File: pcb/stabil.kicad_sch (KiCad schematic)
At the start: 42 parts, among them Q10 IRFR5305, U11 TPS5430DDA, U12 LM75B, U13 INA219AxD, U14 LM78M05_TO252, U16 TSV911IDT, U17 PC817, U18 LM75B

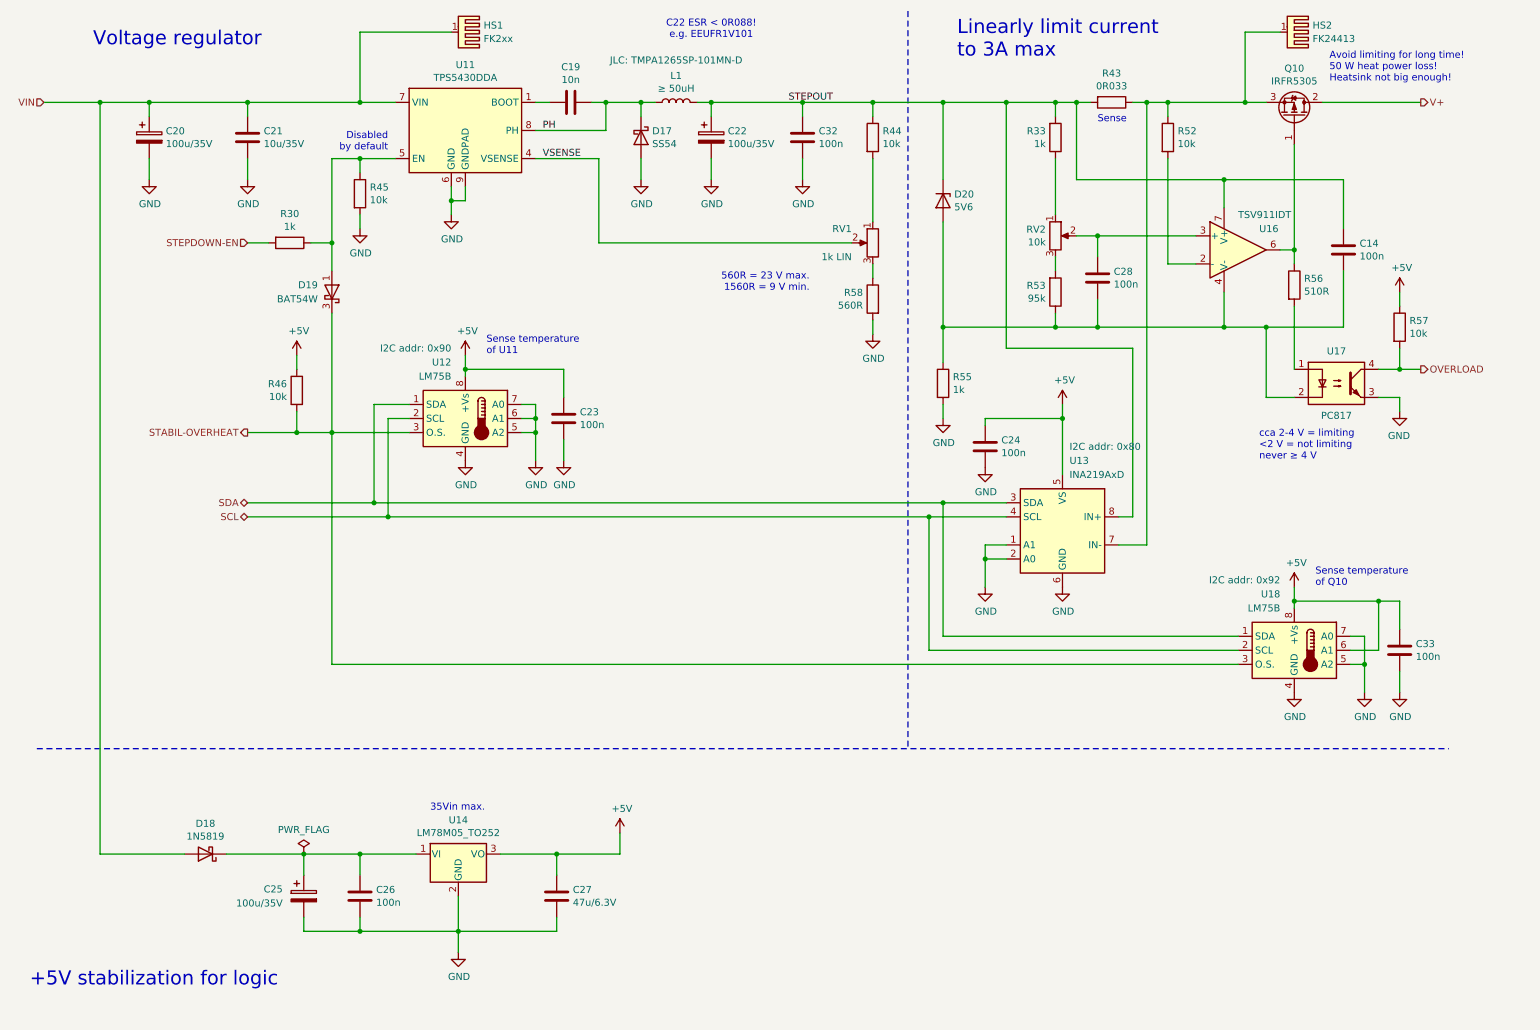
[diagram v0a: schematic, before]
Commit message: Use switched power supply for 5V internal.
78M05 would have 2.5 W of heat loss on it @ 30V input.
Other minor improvements.
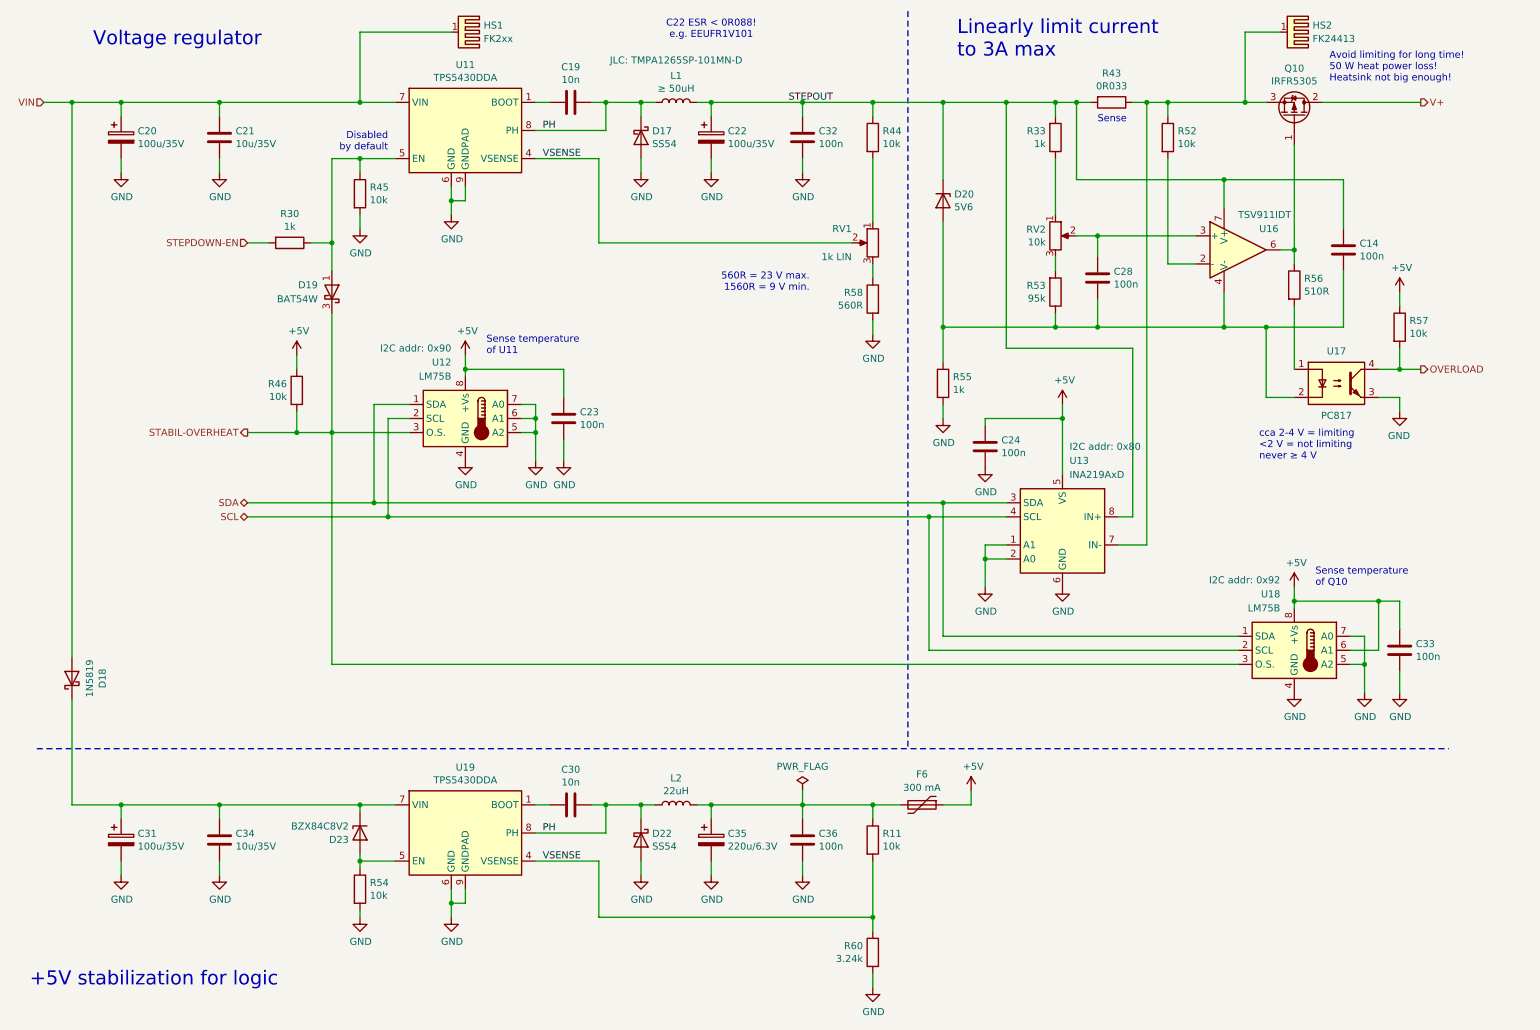
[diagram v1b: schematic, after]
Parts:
- removed C25: 100u/35V, Capacitor_THT:CP_Radial_D6.3mm_P2.50mm, symbol Device:C_Polarized
- removed C26: 100n, Capacitor_SMD:C_0805_2012Metric, symbol Device:C
- removed C27: 47u/6.3V, Capacitor_SMD:C_0805_2012Metric, symbol Device:C
- removed U14: LM78M05_TO252, Package_TO_SOT_SMD:TO-252-2, symbol Regulator_Linear:LM78M05_TO252
- added C30: 10n, Capacitor_SMD:C_0805_2012Metric, symbol Device:C
- added C31: 100u/35V, Capacitor_THT:CP_Radial_D6.3mm_P2.50mm, symbol Device:C_Polarized
- added C34: 10u/35V, Capacitor_SMD:C_0805_2012Metric, symbol Device:C
- added C35: 220u/6.3V, Capacitor_THT:CP_Radial_D8.0mm_P3.50mm, symbol Device:C_Polarized
- added C36: 100n, Capacitor_SMD:C_0805_2012Metric, symbol Device:C
- added D22: SS54, Diode_SMD:D_SMA, symbol Device:D_Schottky
- added D23: BZX84C8V2, Package_TO_SOT_SMD:SOT-23, symbol Diode:BZX84Cxx
- added F6: 300 mA, Fuse:Fuse_2920_7451Metric, symbol Device:Polyfuse
- added L2: 22uH, Inductor_SMD:L_Changjiang_FNR4020S, symbol Device:L
- added R11, R54: 10k, Resistor_SMD:R_0805_2012Metric, symbol Device:R
- added R60: 3.24k, Resistor_SMD:R_0805_2012Metric, symbol Device:R
- added U19: TPS5430DDA, Package_SO:TI_SO-PowerPAD-8_ThermalVias, symbol Regulator_Switching:TPS5430DDA
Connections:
- net +5V: now also F6.1
- net GND: now also C31.2, C34.2, C35.2, C36.2, D22.2 (A), R54.2, R60.2, U19.6 (GND), U19.9 (GNDPAD)
- net PH: now also C30.1, D22.1 (K), L2.1, U19.8 (PH)
- net VSENSE: now also R11.2, R60.1, U19.4 (VSENSE)
- net at D18.1 (K): now also C31.1, C34.1, D23.3 (K), U19.7 (VIN)
- new net: C35.1, C36.1, F6.2, L2.2, R11.1
- new net: D23.1 (A), R54.1, U19.5 (EN)
- new net: C30.2, U19.1 (BOOT)
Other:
- note removed: "35Vin max."
- moved on the sheet: C20, C21, D18
